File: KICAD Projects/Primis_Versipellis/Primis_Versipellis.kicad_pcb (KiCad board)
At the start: 2 copper layers, 50 x 26 mm, 28 parts, among them J2 USB_A, J3 Conn_01x05_Pin, U1 nRF52833_QDxx, Y1 32MHz

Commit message: Gerbers plus clean up
-Added gerbers for the face tracker and versipellis
-Shrunk the face tracker and cleaned up
-Fixed some DRC issues with both projects
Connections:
- net DEC4 renamed DEC4_6

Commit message: Quick Update
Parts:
- Y1: footprint Crystal:Crystal_SMD_5032-2Pin_5.0x3.2mm -> Crystal:Crystal_SMD_2012-2Pin_2.0x1.2mm
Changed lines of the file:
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@@
 		)
 	)
-	(footprint "Crystal:Crystal_SMD_5032-2Pin_5.0x3.2mm"
+	(footprint "Crystal:Crystal_SMD_2012-2Pin_2.0x1.2mm"
 		(layer "F.Cu")
 		(at 160.9 63.5)
-		(descr "SMD2520/2, Crystal, 5.0x3.2mm package, SMD, generated with kicad-footprint-generator make_crystal.py, http://www.icbase.com/File/PDF/HKC/HKC00061008.pdf")
+		(descr "2012/2, Crystal, 2.0x1.2mm package, SMD, generated with kicad-footprint-generator make_crystal.py, http://txccrystal.com/images/pdf/9ht11.pdf")
 		(property "Reference" "Y1"
-			(at -4.35 0 0)
+			(at 0 -1.8 0)
 			(layer "F.SilkS")
 			(effects
@@
 		)
 		(property "Value" "32MHz"
-			(at -4.9 -3 0)
+			(at 0 1.8 0)
 			(layer "F.Fab")
 			(effects
@@
 		(attr smd)
 		(fp_line
-			(start -3.11 -1.86)
-			(end -3.11 1.86)
+			(start -1.26 -0.86)
+			(end -1.26 0.86)
 			(stroke
 				(width 0.12)
@@
 		)
 		(fp_line
-			(start -3.11 1.86)
-			(end 2.76 1.86)
+			(start -1.26 0.86)
+			(end 1.26 0.86)
 			(stroke
 				(width 0.12)
@@
 		)
 		(fp_line
-			(start 2.76 -1.86)
-			(end -3.11 -1.86)
+			(start 1.26 -0.86)
+			(end -1.26 -0.86)
 			(stroke
 				(width 0.12)
@@
 		(fp_circle
 			(center 0 0)
-			(end 0.4 0)
+			(end 0.2 0)
 			(stroke
 				(width 0.1)
@@
 		)
 		(fp_rect
-			(start -3.1 -2.1)
-			(end 3.1 2.1)
+			(start -1.5 -1.1)
+			(end 1.5 1.1)
 			(stroke
 				(width 0.05)
@@
 		(fp_poly
 			(pts
-				(xy 2.5 -1.6) (xy 2.5 1.6) (xy -1.7 1.6) (xy -2.5 0.8) (xy -2.5 -1.6)
+				(xy 1 -0.6) (xy 1 0.6) (xy -0.7 0.6) (xy -1 0.3) (xy -1 -0.6)
 			)
 			(stroke
@@
 			(effects
 				(font
-					(size 1 1)
-					(thickness 0.15)
+					(size 0.5 0.5)
+					(thickness 0.08)
 				)
 			)
 		)
 		(pad "1" smd roundrect
-			(at -1.85 0)
-			(size 2 2.4)
+			(at -0.7 0)
+			(size 0.6 1.1)
 			(layers "F.Cu" "F.Mask" "F.Paste")
-			(roundrect_rratio 0.125)
+			(roundrect_rratio 0.25)
 			(net 5 "Net-(U1-XC1)")
 			(pinfunction "1")
@@
 		)
 		(pad "2" smd roundrect
-			(at 1.85 0)
-			(size 2 2.4)
+			(at 0.7 0)
+			(size 0.6 1.1)
 			(layers "F.Cu" "F.Mask" "F.Paste")
-			(roundrect_rratio 0.125)
+			(roundrect_rratio 0.25)
 			(net 4 "Net-(U1-XC2)")
 			(pinfunction "2")
@@
 		)
 		(embedded_fonts no)
-		(model "${KICAD9_3DMODEL_DIR}/Crystal.3dshapes/Crystal_SMD_5032-2Pin_5.0x3.2mm.step"
+		(model "${KICAD9_3DMODEL_DIR}/Crystal.3dshapes/Crystal_SMD_2012-2Pin_2.0x1.2mm.step"
 			(offset
 				(xyz 0 0 0)
@@
 	)
 	(segment
-		(start 162.75 63.5)
-		(end 162.75 61.475)
+		(start 161.775 60.5)
+		(end 161.775 63.325)
 		(width 0.2)
 		(layer "F.Cu")
@@
 	)
 	(segment
-		(start 162.75 61.475)
-		(end 161.775 60.5)
+		(start 161.775 63.325)
+		(end 161.6 63.5)
 		(width 0.2)
 		(layer "F.Cu")
@@
 	)
 	(segment
-		(start 160 64.45)
-		(end 159.05 63.5)
+		(start 160 66.5)
+		(end 160 63.7)
 		(width 0.2)
 		(layer "F.Cu")
@@
 	)
 	(segment
-		(start 160 66.5)
-		(end 160 64.45)
-		(width 0.2)
-		(layer "F.Cu")
+		(start 160 63.7)
+		(end 160.2 63.5)
+		(width 0.2)
+		(layer "F.Cu")

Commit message: FaceTracker fixes and Dongle rework
-Fixed some mistakes on the Facetracker with the camera power lines.
-Some part swaps and additions on the dongle to match the JLCPCBs catalogue
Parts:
- removed R3: 1.0k, Resistor_SMD:R_0603_1608Metric
- removed Y1: 32MHz, Crystal:Crystal_SMD_2012-2Pin_2.0x1.2mm
- added C12: 100nF, Capacitor_SMD:C_0603_1608Metric, F.Cu at (139.2, 60.6)
- added R2: 10k, Resistor_SMD:R_0603_1608Metric, F.Cu at (139.9, 66.8)
- added Y2: Crystal_GND24, Crystal:Crystal_SMD_Abracon_ABM8G-4Pin_3.2x2.5mm, F.Cu at (164.5, 63.6)
- D3: value LED -> WS2812B-2020; footprint LED_SMD:LED_0603_1608Metric -> LED_SMD:LED_WS2812B-2020_PLCC4_2.0x2.0mm
- moved R1 14.8 mm to (155.4, 60.6), turned to 0 degrees
- moved D1 9.95 mm to (155.4, 58.8)
- moved D3 1.58 mm to (144.3, 59.9), turned to 0 degrees
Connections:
- D3 pad 1: Net-(D3-K) -> unconnected-(D3-DOUT-Pad1)
- D3 pad 2: Net-(D3-A) -> GND
- U1 pad 16: Net-(J3-Pin_3) -> Net-(U1-P0.18/~{RESET})
- U1 pad 35: Net-(D3-K) -> Net-(D3-DIN)
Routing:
- net Net-(U1-P0.18/~{RESET}): track 0.00 -> 20.1 mm, vias 0 -> 2
- net Net-(J3-Pin_3): track 22.6 -> 2.89 mm, vias 2 -> 0
- net Net-(D3-DIN): track 0.00 -> 14.3 mm
- net Net-(D3-K): track 13.6 -> 0.00 mm
- net Net-(D3-VDD): track 0.00 -> 6.21 mm
- net GND: track 39.1 -> 44.2 mm, vias 29 -> 32
- net Net-(D3-A): track 3.00 -> 0.00 mm
- net Net-(U1-XC2): track 15.4 -> 17.1 mm
- net Net-(U1-XC1): track 9.97 -> 11.3 mm
- net Net-(D1-A): track 3.07 -> 1.80 mm

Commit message: Usb swap
-Changed the dongle to another usb
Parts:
- J2: footprint Connector_USB:USB_A_CNCTech_1001-011-01101_Horizontal -> USB:USB05
- moved J2 9.51 mm to (129.4, 66.0), turned to -90 degrees
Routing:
- net VBUS: track 12.1 -> 15.7 mm, vias 1 -> 0
- net D-: track 34.6 -> 32.6 mm

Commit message: Dongle Cleanup
-CLeanup before final
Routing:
- net GND: track 44.5 -> 38.7 mm, vias 32 -> 30
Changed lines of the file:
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@@
-	)
-	(segment
-		(start 127.5 63.5)
-		(end 129.5 61.5)
-		(width 0.5)
-		(layer "F.Cu")
-		(net "GND")
 	)
 	(segment
@@
 	)
 	(segment
-		(start 127.5 75.5)
-		(end 129.5 77.5)
-		(width 0.5)
-		(layer "F.Cu")
-		(net "GND")
-	)
-	(segment
 		(start 145.275 71.5)
 		(end 144 71.5)
@@
 	)
 	(segment
-		(start 127.442 63.5)
-		(end 127.5 63.5)
-		(width 0.5)
-		(layer "F.Cu")
-		(net "GND")
-	)
-	(segment
 		(start 145.275 69.5)
 		(end 144 69.5)
@@
 		(net "GND")
 	)
-	(segment
-		(start 127.442 75.5)
-		(end 127.5 75.5)
-		(width 0.5)
-		(layer "F.Cu")
-		(net "GND")
-	)
 	(via
 		(at 132.5 73)
@@
 	)
 	(via
-		(at 129.5 77.5)
-		(size 0.6)
-		(drill 0.3)
-		(layers "F.Cu" "B.Cu")
-		(net "GND")
-	)
-	(via
 		(at 144 62.5)
 		(size 0.7)
@@
 		(net "GND")
 	)
-	(via
-		(at 129.5 61.5)
-		(size 0.6)
-		(drill 0.3)
-		(layers "F.Cu" "B.Cu")
-		(net "GND")
-	)

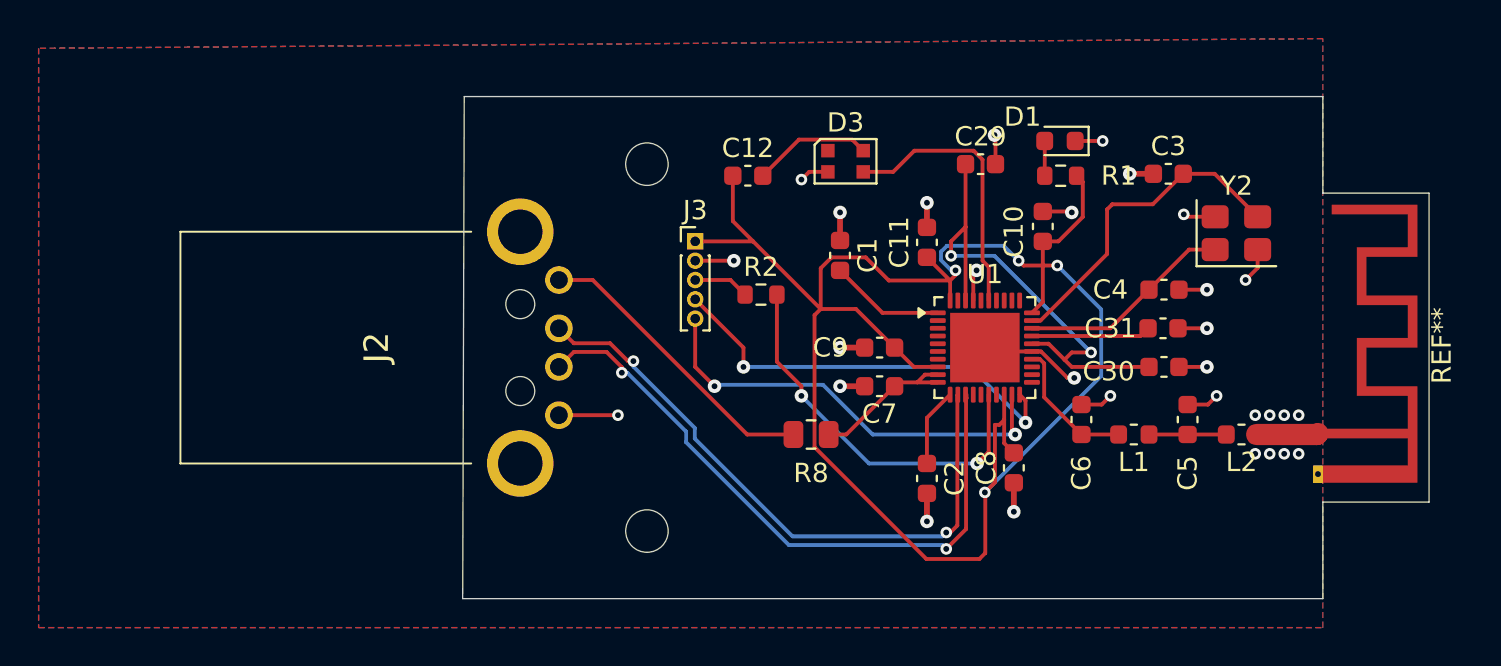
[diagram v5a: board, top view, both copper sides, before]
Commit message: Versipellis EV1 Final + General Github updates
-Fixed a few remaining issues with Versipellis EV1
-Created production files for Versipellis
-Updated pictures for all projects
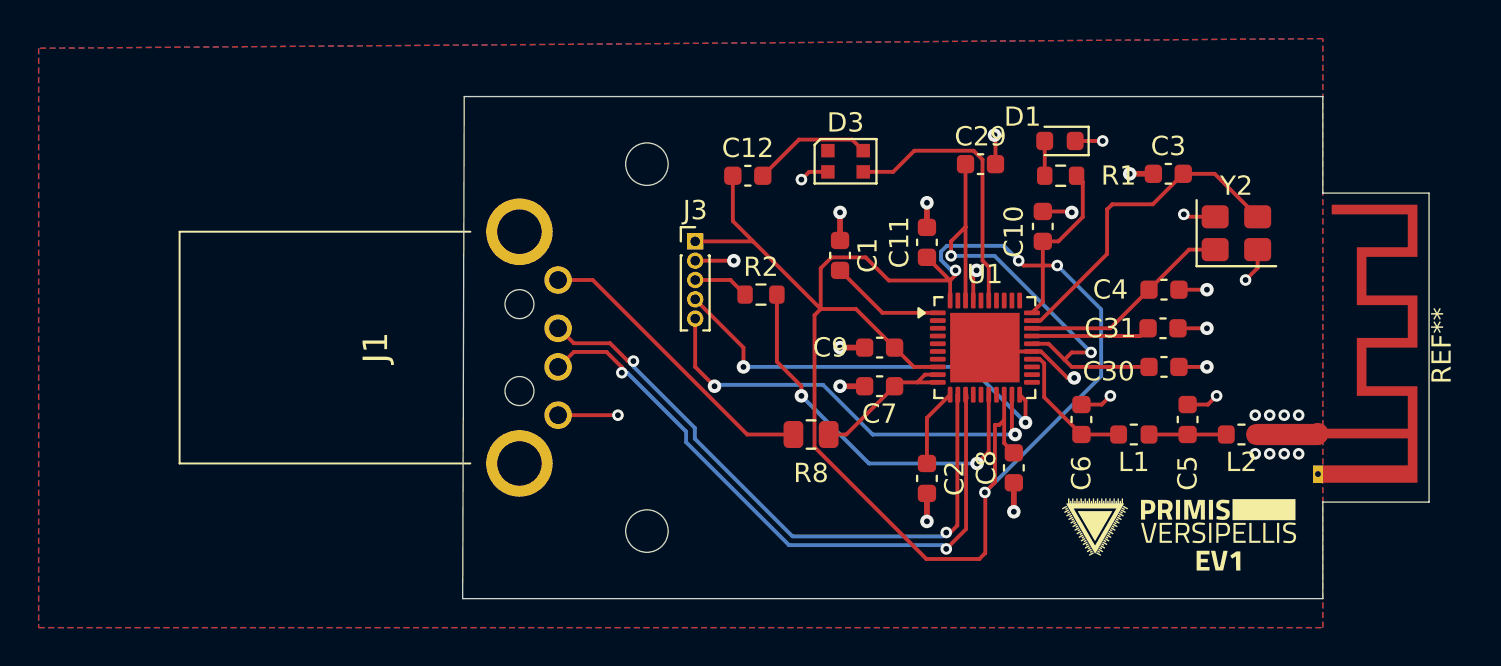
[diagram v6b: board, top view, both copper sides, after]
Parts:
- removed J2: USB_A, USB:USB05
- added G***: LOGO, LOGO, F.Cu at (163.6, 79.2)
- added G***: LOGO, LOGO, F.Cu at (157.2, 78.8)
- added J1: USB-05, Veri:USB05, F.Cu at (129.4, 66.0)

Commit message: Quick EV1 Dongle Fixes
-Made some last minute fixes
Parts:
- J3: footprint Connector_PinHeader_1.00mm:PinHeader_1x05_P1.00mm_Vertical -> Connector_PinHeader_1.27mm:PinHeader_1x05_P1.27mm_Vertical
- moved J3 0.22 mm to (136.6, 63.8)
- moved J1 0.20 mm to (129.6, 66.0)
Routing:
- net Net-(J3-Pin_5): track 22.7 -> 21.8 mm
- net VDD_nRF: track 93.3 -> 92.5 mm
- net Net-(J3-Pin_4): track 21.9 -> 21.2 mm
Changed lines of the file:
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@@
 		)
 	)
-	(footprint "Connector_PinHeader_1.00mm:PinHeader_1x05_P1.00mm_Vertical"
+	(footprint "Connector_PinHeader_1.27mm:PinHeader_1x05_P1.27mm_Vertical"
 		(layer "F.Cu")
-		(at 136.5 64)
-		(descr "Through hole straight pin header, 1x05, 1.00mm pitch, single row")
-		(tags "Through hole pin header THT 1x05 1.00mm single row")
+		(at 136.6 63.8)
+		(descr "Through hole straight pin header, 1x05, 1.27mm pitch, single row")
+		(tags "Through hole pin header THT 1x05 1.27mm single row")
 		(property "Reference" "J3"
-			(at 0 -1.61 0)
+			(at 0 -1.745 0)
 			(layer "F.SilkS")
 			(effects
@@
 		)
 		(property "Value" "Conn_01x05_Pin"
-			(at 0 5.61 0)
+			(at 0 6.825 0)
 			(layer "F.Fab")
 			(effects
@@
 				(font
 					(size 1.27 1.27)
-					(thickness 0.15)
 				)
 			)
@@
 				(font
 					(size 1.27 1.27)
+				)
+			)
+		)
+		(property "KiLib_Generator" "connector/pin_header_socket"
+			(at 0 0 0)
+			(layer "F.SilkS")
+			(hide yes)
+			(effects
+				(font
+					(size 1 1)
 					(thickness 0.15)
 				)
@@
 		(duplicate_pad_numbers_are_jumpers no)
 		(fp_line
-			(start -0.745 -0.735)
-			(end 0 -0.735)
+			(start -1.16 -0.81)
+			(end 0 -0.81)
 			(stroke
 				(width 0.12)
@@
 		)
 		(fp_line
-			(start -0.745 0)
-			(end -0.745 -0.735)
+			(start -1.16 0)
+			(end -1.16 -0.81)
 			(stroke
 				(width 0.12)
@@
 		)
 		(fp_line
-			(start -0.745 0.735)
-			(end -0.745 4.61)
+			(start -1.16 0.81)
+			(end -1.16 5.825)
 			(stroke
 				(width 0.12)
@@
 		)
 		(fp_line
-			(start -0.745 0.735)
-			(end -0.685565 0.735)
+			(start -1.16 0.81)
+			(end -0.666708 0.81)
 			(stroke
 				(width 0.12)
@@
 		)
 		(fp_line
-			(start -0.745 4.61)
-			(end -0.41003 4.61)
+			(start -1.16 5.825)
+			(end -0.317923 5.825)
 			(stroke
 				(width 0.12)
@@
 		)
 		(fp_line
-			(start 0.41003 4.61)
-			(end 0.745 4.61)
+			(start 0.317923 5.825)
+			(end 1.16 5.825)
 			(stroke
 				(width 0.12)
@@
 		)
 		(fp_line
-			(start 0.685565 0.735)
-			(end 0.745 0.735)
+			(start 0.666708 0.81)
+			(end 1.16 0.81)
 			(stroke
 				(width 0.12)
@@
 		)
 		(fp_line
-			(start 0.745 0.735)
-			(end 0.745 4.61)
+			(start 1.16 0.81)
+			(end 1.16 5.825)
 			(stroke
 				(width 0.12)
@@
 		)
 		(fp_rect
-			(start -1.14 -1)
-			(end 1.14 5)
+			(start -1.55 -1.14)
+			(end 1.55 6.22)
 			(stroke
 				(width 0.05)
@@
 		)
 		(fp_line
-			(start -0.635 -0.1825)
-			(end -0.3175 -0.5)
+			(start -1.05 -0.11)
+			(end -0.525 -0.635)
 			(stroke
 				(width 0.1)
@@
 		)
 		(fp_line
-			(start -0.635 4.5)
-			(end -0.635 -0.1825)
+			(start -1.05 5.715)
+			(end -1.05 -0.11)
 			(stroke
 				(width 0.1)
@@
 		)
 		(fp_line
-			(start -0.3175 -0.5)
-			(end 0.635 -0.5)
+			(start -0.525 -0.635)
+			(end 1.05 -0.635)
 			(stroke
 				(width 0.1)
@@
 		)
 		(fp_line
-			(start 0.635 -0.5)
-			(end 0.635 4.5)
+			(start 1.05 -0.635)
+			(end 1.05 5.715)
 			(stroke
 				(width 0.1)
@@
 		)
 		(fp_line
-			(start 0.635 4.5)
-			(end -0.635 4.5)
+			(start 1.05 5.715)
+			(end -1.05 5.715)
 			(stroke
 				(width 0.1)
@@
 		)
 		(fp_text user "${REFERENCE}"
-			(at 0 2 90)
+			(at 0 2.54 90)
 			(layer "F.Fab")
 			(effects
 				(font
-					(size 0.76 0.76)
-					(thickness 0.114)
+					(size 1 1)
+					(thickness 0.15)
 				)
 			)
@@
 		(pad "1" thru_hole rect
 			(at 0 0)
-			(size 0.85 0.85)
-			(drill 0.5)
+			(size 1 1)
+			(drill 0.65)
 			(layers "*.Cu" "*.Mask")
 			(remove_unused_layers no)
@@
 		)
 		(pad "2" thru_hole circle
-			(at 0 1)
-			(size 0.85 0.85)
-			(drill 0.5)
+			(at 0 1.27)
+			(size 1 1)
+			(drill 0.65)
 			(layers "*.Cu" "*.Mask")
 			(remove_unused_layers no)
@@
 		)
 		(pad "3" thru_hole circle
-			(at 0 2)
-			(size 0.85 0.85)
-			(drill 0.5)
+			(at 0 2.54)
+			(size 1 1)
+			(drill 0.65)
 			(layers "*.Cu" "*.Mask")
 			(remove_unused_layers no)
@@
 		)
 		(pad "4" thru_hole circle
-			(at 0 3)
-			(size 0.85 0.85)
-			(drill 0.5)
+			(at 0 3.81)
+			(size 1 1)
+			(drill 0.65)
 			(layers "*.Cu" "*.Mask")
 			(remove_unused_layers no)
@@
 		)
 		(pad "5" thru_hole circle
-			(at 0 4)
-			(size 0.85 0.85)
-			(drill 0.5)
+			(at 0 5.08)
+			(size 1 1)
+			(drill 0.65)
 			(layers "*.Cu" "*.Mask")
 			(remove_unused_layers no)
@@
 		)
 		(embedded_fonts no)
-		(model "${KICAD9_3DMODEL_DIR}/Connector_PinHeader_1.00mm.3dshapes/PinHeader_1x05_P1.00mm_Vertical.step"
+		(model "${KICAD10_3DMODEL_DIR}/Connector_PinHeader_1.27mm.3dshapes/PinHeader_1x05_P1.27mm_Vertical.step"
 			(offset
 				(xyz 0 0 0)
@@
 	(footprint "Veri:USB05"
 		(layer "F.Cu")
-		(at 129.4 66 -90)
+		(at 129.6 66 -90)
 		(descr "USB-05-4")
 		(tags "Connector")
@@
 		)
 		(embedded_fonts no)
-		(model "/home/cody/Documents/GitHub/FrameWork/KICAD Projects/_Shared/Models/USB-05.stp"
+		(model "/home/cody/Documents/GitHub/FrameWork/KICAD Projects/_Shared/Models/USB Connector Type A male, SMT.STEP"
 			(offset
-				(xyz 0 0 0)
+				(xyz 3.5 -20 2)
 			)
 			(scale
@@
 			)
 			(rotate
-				(xyz 0 0 0)
+				(xyz -90 -0 -0)
 			)
 		)
@@
 	)
 	(segment
-		(start 136.5 65)
-		(end 138.5 65)
-		(width 0.2)
+		(start 148.5 77.05)
+		(end 148.5 78.5)
+		(width 0.3)
 		(layer "F.Cu")
 		(net "GND")
 	)
 	(segment
-		(start 148.5 77.05)
-		(end 148.5 78.5)
-		(width 0.3)
+		(start 138.73 65.07)
+		(end 138.8 65)
+		(width 0.2)
 		(layer "F.Cu")
 		(net "GND")
@@
 	)
 	(segment
+		(start 136.6 65.07)
+		(end 138.73 65.07)
+		(width 0.2)
+		(layer "F.Cu")
+		(net "GND")
+	)
+	(segment
 		(start 160.225 60.5)
 		(end 159 60.5)
@@
 	)
 	(via
-		(at 138.5 65)
-		(size 0.7)
-		(drill 0.3)
-		(layers "F.Cu" "B.Cu")
-		(capping no)
-		(covering
-			(front no)
-			(back no)
-		)
-		(plugging
-			(front no)
-			(back no)
-		)
-		(filling no)
-		(net "GND")
-	)
-	(via
 		(at 144 69.5)
 		(size 0.7)
@@
 	)
 	(via
+		(at 138.8 65)
+		(size 0.6)
+		(drill 0.3)
+		(layers "F.Cu" "B.Cu")
+		(net "GND")
+	)
+	(via
 		(at 144 71.5)
 		(size 0.7)
@@
 	)
 	(segment
-		(start 152.5 73.25)
-		(end 152.5 71.9375)
+		(start 136.6 63.8)
+		(end 137.6 63.8)
 		(width 0.2)
 		(layer "F.Cu")
@@
 	)
 	(segment
-		(start 148.472978 80.446)
-		(end 142.679 74.652022)
+		(start 152.5 73.25)
+		(end 152.5 71.9375)
 		(width 0.2)
 		(layer "F.Cu")
@@
 	)
 	(segment
-		(start 136.5 64)
-		(end 139.5 64)
+		(start 148.472978 80.446)
+		(end 142.679 74.652022)
 		(width 0.2)
 		(layer "F.Cu")
@@
 	)
 	(segment
+		(start 137.6 63.8)
+		(end 138.45 62.95)
+		(width 0.2)
+		(layer "F.Cu")
+		(net "VDD_nRF")
+	)
+	(segment
 		(start 146.525 66.025)
 		(end 145.329 64.829)
@@
 	)
 	(segment
-		(start 136.5 66)
-		(end 138.325 66)
+		(start 139.08 66.755)
+		(end 137.015 66.755)
 		(width 0.2)
 		(layer "F.Cu")
@@
 	)
 	(segment
-		(start 138.325 66)
-		(end 139.08 66.755)
+		(start 137.015 66.755)
+		(end 136.6 66.34)
 		(width 0.2)
 		(layer "F.Cu")
@@
 	)
 	(segment
-		(start 139 69.5)
-		(end 139 70.5)
+		(start 139 70.01)
+		(end 136.6 67.61)
 		(width 0.2)
 		(layer "F.Cu")
@@
 	)
 	(segment
-		(start 136.5 67)
-		(end 139 69.5)
+		(start 139 70.5)
+		(end 139 70.01)
 		(width 0.2)
 		(layer "F.Cu")
@@
 	)
 	(segment
-		(start 136.5 68)
-		(end 136.5 70.5)
+		(start 137.5 71.5)
+		(end 136.6 70.6)
 		(width 0.2)
 		(layer "F.Cu")
@@
 	)
 	(segment
-		(start 136.5 70.5)
-		(end 137.5 71.5)
+		(start 136.6 70.6)
+		(end 136.6 68.88)
 		(width 0.2)
 		(layer "F.Cu")
